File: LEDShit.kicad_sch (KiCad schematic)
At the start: 134 parts, among them U4 74AHCT1G125

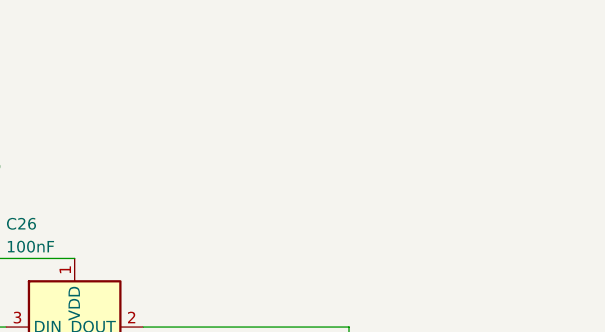
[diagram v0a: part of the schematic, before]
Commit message: Filename Changes
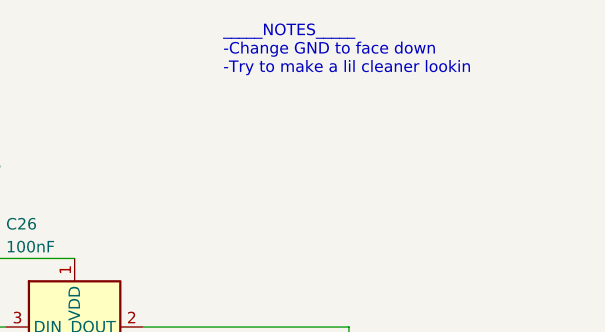
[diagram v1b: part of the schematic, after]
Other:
- note added: "_____NOTES_____ -Change GND to face down -Try to make a lil cleaner lookin"
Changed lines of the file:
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@@
     (stroke (width 0) (type default))
+  )
+  (text "_____NOTES_____\n-Change GND to face down\n-Try to make a lil cleaner lookin"
+    (at 355.6 25.4 0)
+    (effects (font (size 1.27 1.27)) (justify left bottom))
   )
   (global_label "LED_DATAO" (shape input) (at 367.03 223.52 0) (fields_autoplaced)
